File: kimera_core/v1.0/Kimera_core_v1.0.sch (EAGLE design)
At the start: 21 parts, among them IC1 PCA9555RGER-NOPAD, IC2 PCA9555RGER-NOPAD, Q1 CSTCR6M00G53Z, U1 ATMEGA32U4QFN2

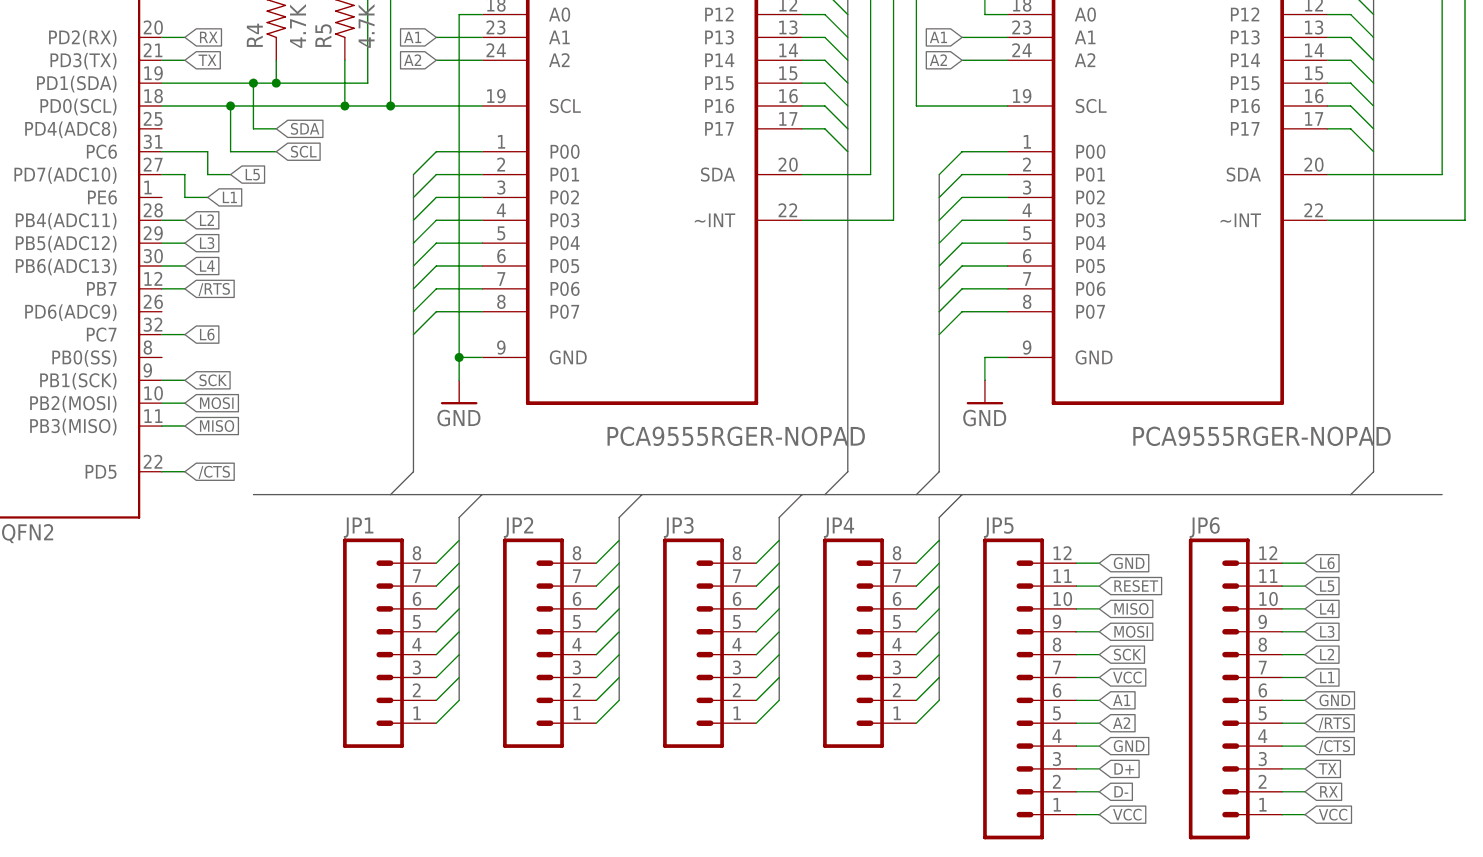
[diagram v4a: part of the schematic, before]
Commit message: kimera_core: Reduce board size and remove some main io
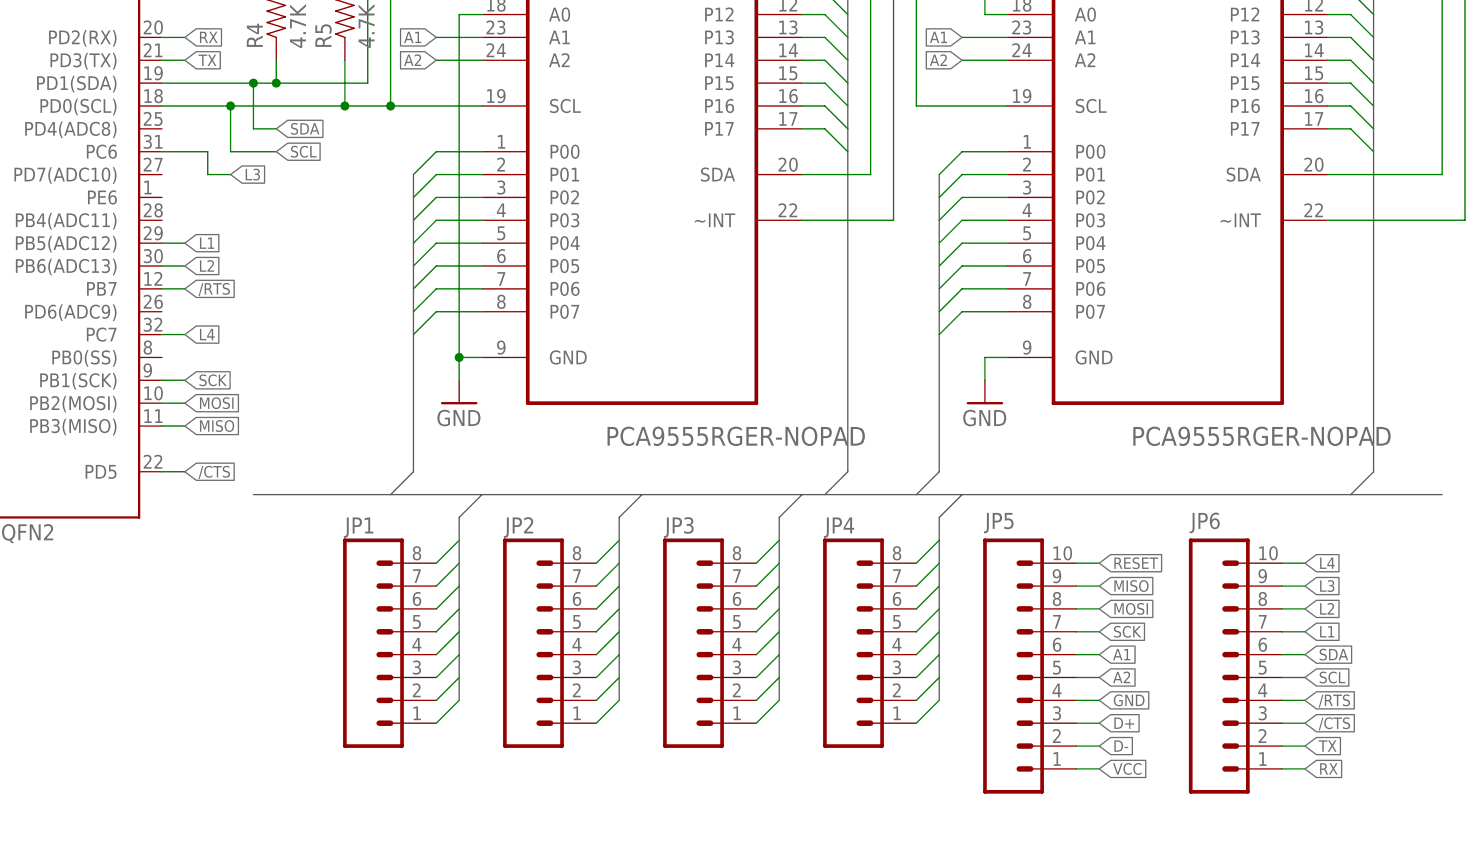
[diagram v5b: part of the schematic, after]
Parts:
- JP5, JP6: device castellation:P12 -> castellation:P10
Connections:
- removed net L5: JP6.11, U1.PC6
- removed net L6: JP6.12, U1.PC7
- net /CTS: now also JP6.3; no longer JP6.4
- net /RTS: now also JP6.4; no longer JP6.5
- net GND: no longer JP5.12, JP6.6
- net L1: now also U1.PB5(ADC12); no longer U1.PD7(ADC10)
- net L2: now also U1.PB6(ADC13); no longer U1.PB4(ADC11)
- net L3: now also U1.PC6; no longer U1.PB5(ADC12)
- net L4: now also U1.PC7; no longer U1.PB6(ADC13)
- net MISO: now also JP5.9; no longer JP5.10
- net MOSI: now also JP5.8; no longer JP5.9
- net RESET: now also JP5.10; no longer JP5.11
- net RX: now also JP6.1; no longer JP6.2
- net SCK: now also JP5.7; no longer JP5.8
- net SCL: now also JP6.5
- net SDA: now also JP6.6
- net TX: now also JP6.2; no longer JP6.3
- net VCC: no longer JP5.7, JP6.1

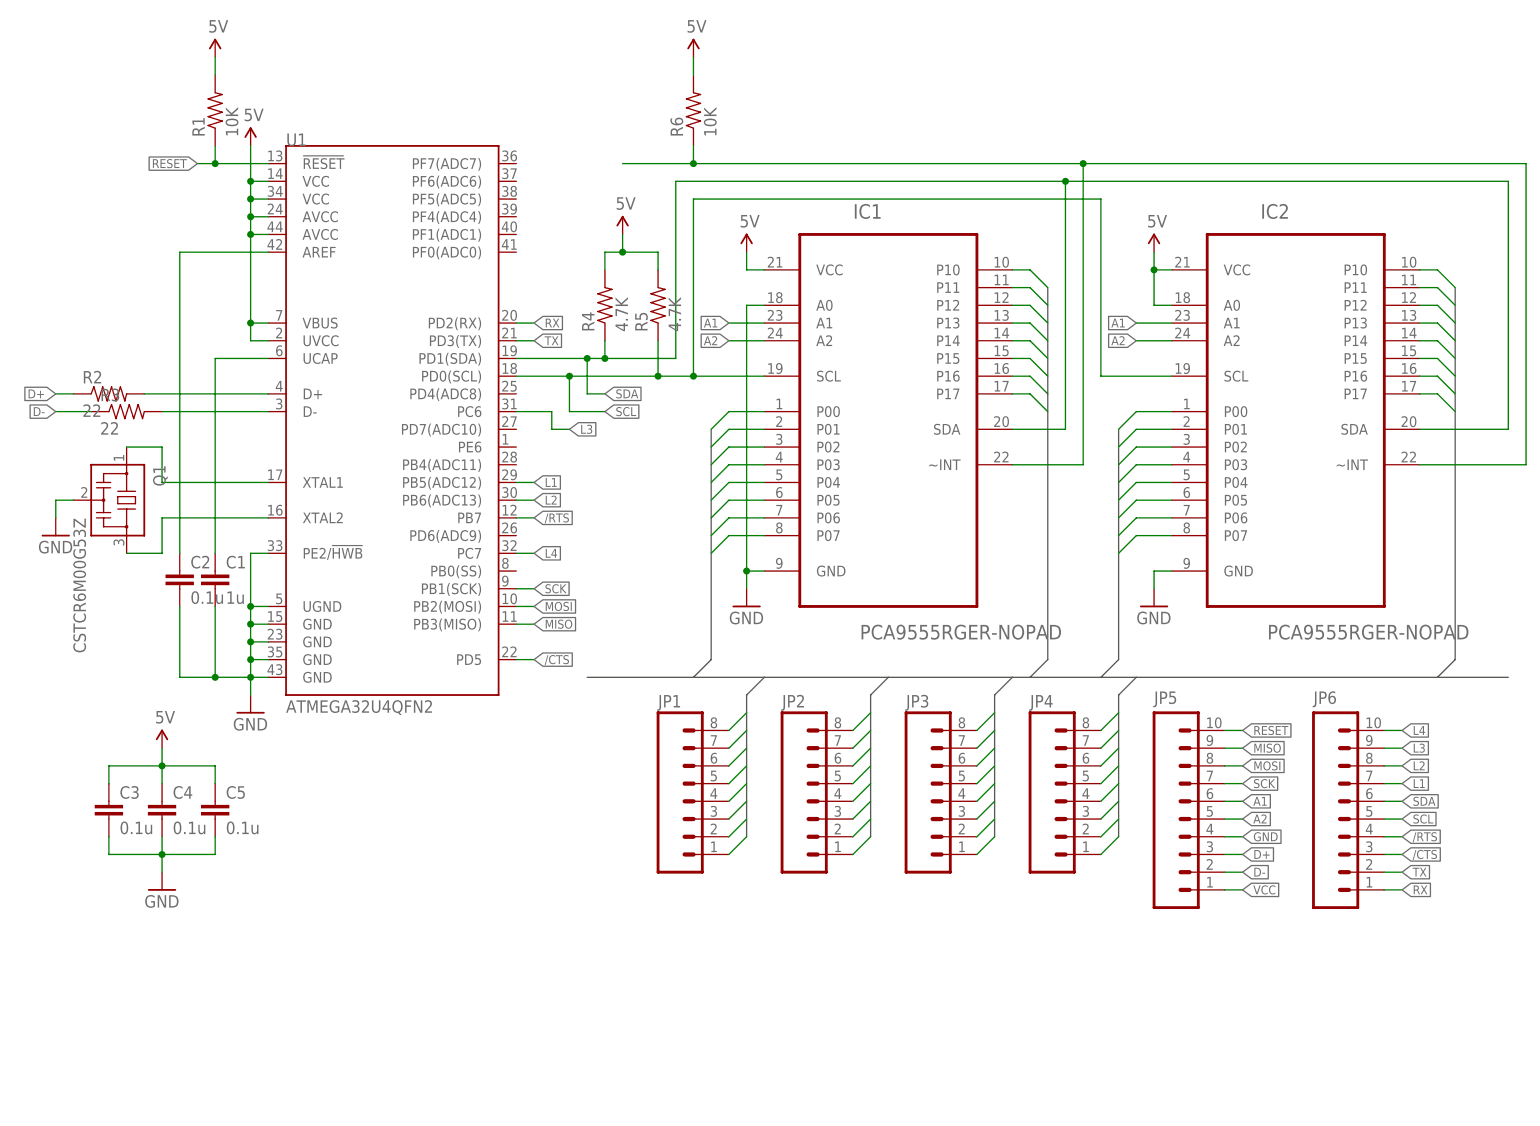
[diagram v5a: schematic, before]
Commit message: kimera_core: First complete version - Finish routing - Add logo and silk screen
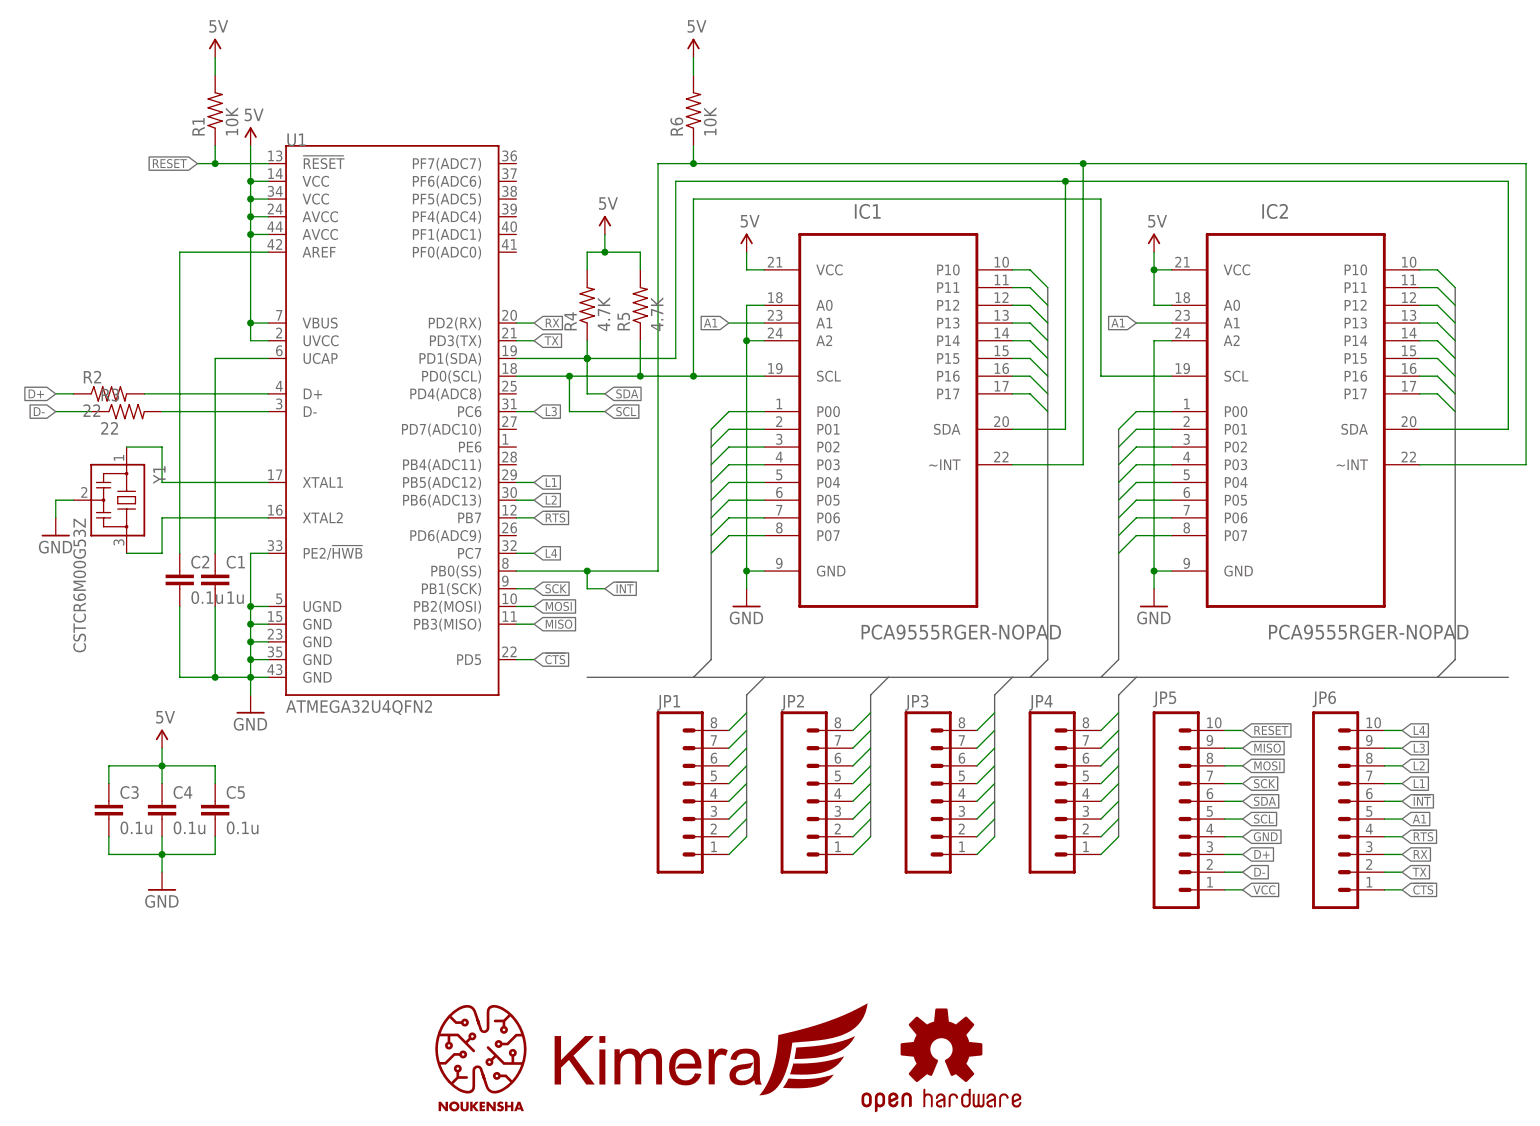
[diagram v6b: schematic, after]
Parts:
- added LOGO1: KIMERA_LOGO, logo:KIMERA_LOGO
- added LOGO2: NOUKENSHA_LOGONIX, logo:NOUKENSHA_LOGONIX
- added LOGO3: OSHW_LOGONIX, logo:OSHW_LOGONIX
- renumbered Q1 to Y1
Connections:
- net /RTS renamed !RTS
- removed net /CTS: JP6.3, U1.PD5
- removed net A2: IC1.A2, IC2.A2, JP5.5
- removed net N$12: IC1.~INT, IC2.~INT, R6.1
- new net !CTS: JP6.1, U1.PD5
- new net !INT: IC1.~INT, IC2.~INT, JP6.6, R6.1, U1.PB0(SS)
- net A1: now also JP6.5; no longer JP5.6
- net GND: now also IC1.A2, IC2.A2
- net RX: now also JP6.3; no longer JP6.1
- net SCL: now also JP5.5; no longer JP6.5
- net SDA: now also JP5.6; no longer JP6.6
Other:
- moved on the sheet: R4, R5
